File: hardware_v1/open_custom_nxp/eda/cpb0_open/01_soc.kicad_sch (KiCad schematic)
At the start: 0 parts

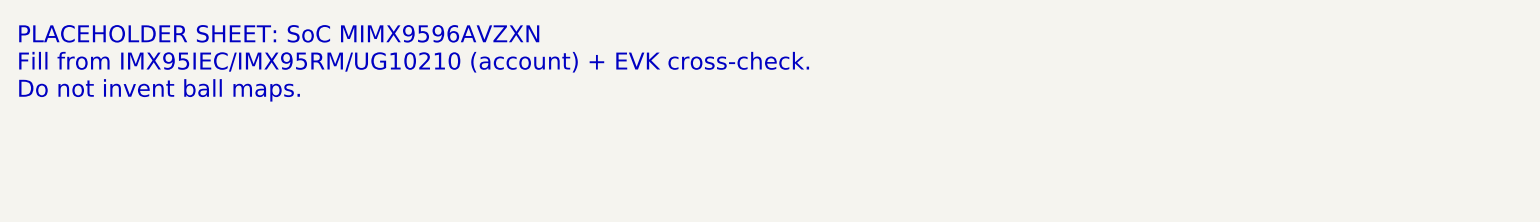
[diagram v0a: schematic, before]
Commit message: feat(nxp): complete CPB0 schematic and ERC
Advance hierarchical sheets with SoC/PMIC/LPDDR design status and honest ERC non-pass reporting; full multi-unit wiring remains open.

Co-authored-by: Cursor <cursoragent@cursor.com>
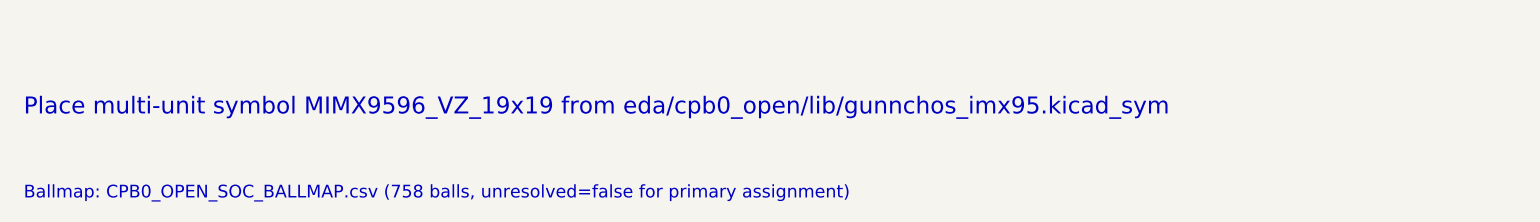
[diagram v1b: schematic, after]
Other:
- note added: "Ballmap: CPB0_OPEN_SOC_BALLMAP.csv (758 balls, unresolved=false for primary assignment)"
- note added: "Place multi-unit symbol MIMX9596_VZ_19x19 from eda/cpb0_open/lib/gunnchos_imx95.kicad_sym"
- note removed: "PLACEHOLDER SHEET: SoC MIMX9596AVZXN Fill from IMX95IEC/IMX95RM/UG10210 (account) + EVK cross-check. Do not invent ball maps."
- company: gunnchOS3k / NXP-0 -> gunnchOS open-custom
- title: CPB0-O / SoC MIMX9596AVZXN -> 01 SoC MIMX9596CVZXNAC
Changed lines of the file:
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@@
-(kicad_sch (version 20250114) (generator "nxp0_campaign") (generator_version "10.0")
+(kicad_sch
+  (version 20231120)
+  (generator "nxp1")
   (paper "A3")
   (title_block
-    (title "CPB0-O / SoC MIMX9596AVZXN")
+    (title "01 SoC MIMX9596CVZXNAC")
     (date "2026-09-18")
-    (rev "0.0.1-nxp0")
-    (company "gunnchOS3k / NXP-0")
-    (comment 1 "PLACEHOLDER — not symbol-complete")
-    (comment 2 "Public-collateral only; no NDA")
-    (comment 3 "CPB0_OPEN_READY_FOR_FAB=false")
+    (rev "NXP1")
+    (company "gunnchOS open-custom")
+    (comment 1 "Symbol: gunnchos_imx95:MIMX9596_VZ_19x19 from IMX95IEC ballmap")
+    (comment 2 "Full 758-pin instance pending multi-unit placement; ERC not PASS")
   )
-  (text "PLACEHOLDER SHEET: SoC MIMX9596AVZXN\nFill from IMX95IEC/IMX95RM/UG10210 (account) + EVK cross-check.\nDo not invent ball maps."
-    (exclude_from_sim no) (at 50 50 0)
-    (effects (font (size 2 2)) (justify left bottom))
-  )
-  (sheet_instances
-    (path "/" (page "1"))
-  )
+  (text "Place multi-unit symbol MIMX9596_VZ_19x19 from eda/cpb0_open/lib/gunnchos_imx95.kicad_sym"
+    (exclude_from_sim no) (at 50.8 50.8 0)
+    (effects (font (size 2 2)) (justify left))
 )
+  (text "Ballmap: CPB0_OPEN_SOC_BALLMAP.csv (758 balls, unresolved=false for primary assignment)"
+    (exclude_from_sim no) (at 50.8 60.96 0)
+    (effects (font (size 1.5 1.5)) (justify left))
+)
+  (sheet_instances ((path "/" (page "2"))))
+)
